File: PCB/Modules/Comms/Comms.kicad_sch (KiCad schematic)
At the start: 25 parts, among them J1 In, J2 ESP32, J3 Bus, J4 Bus, SW1 RUN/~{PROG}, U1 DS1390U, U2 THVD1420D, U3 WiFi / BLE, Y1 32.767kHz

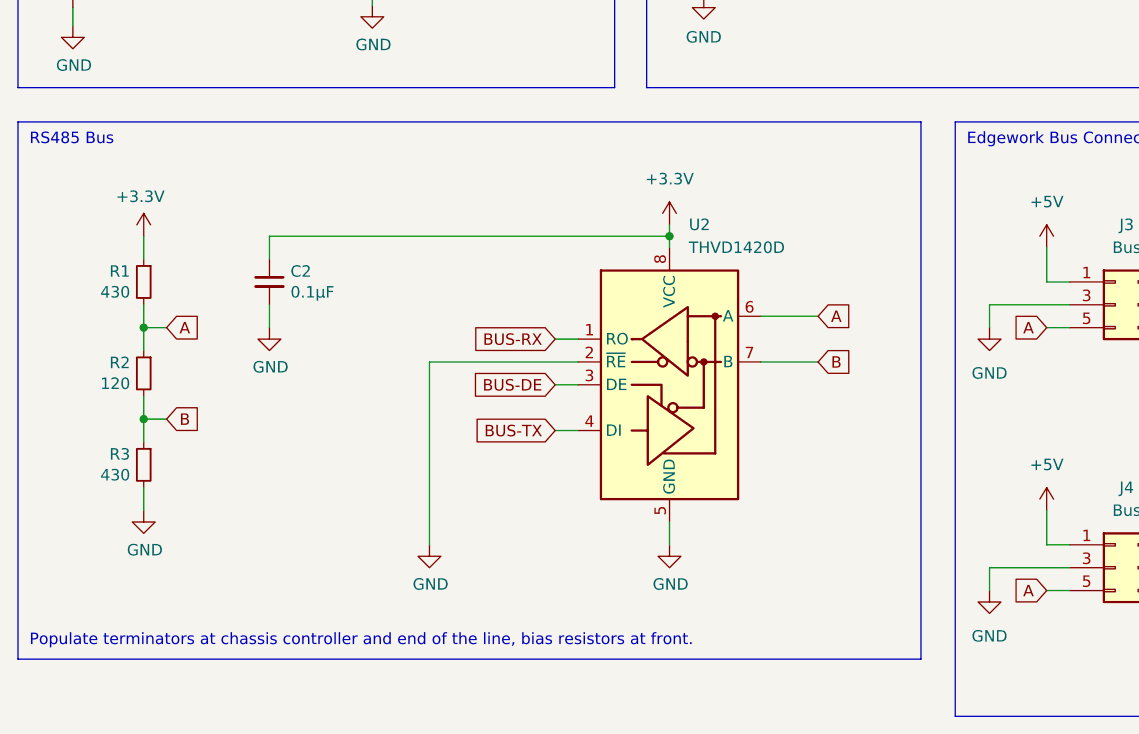
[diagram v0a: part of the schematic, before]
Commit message: Add ESD protection to the RS485 networks.
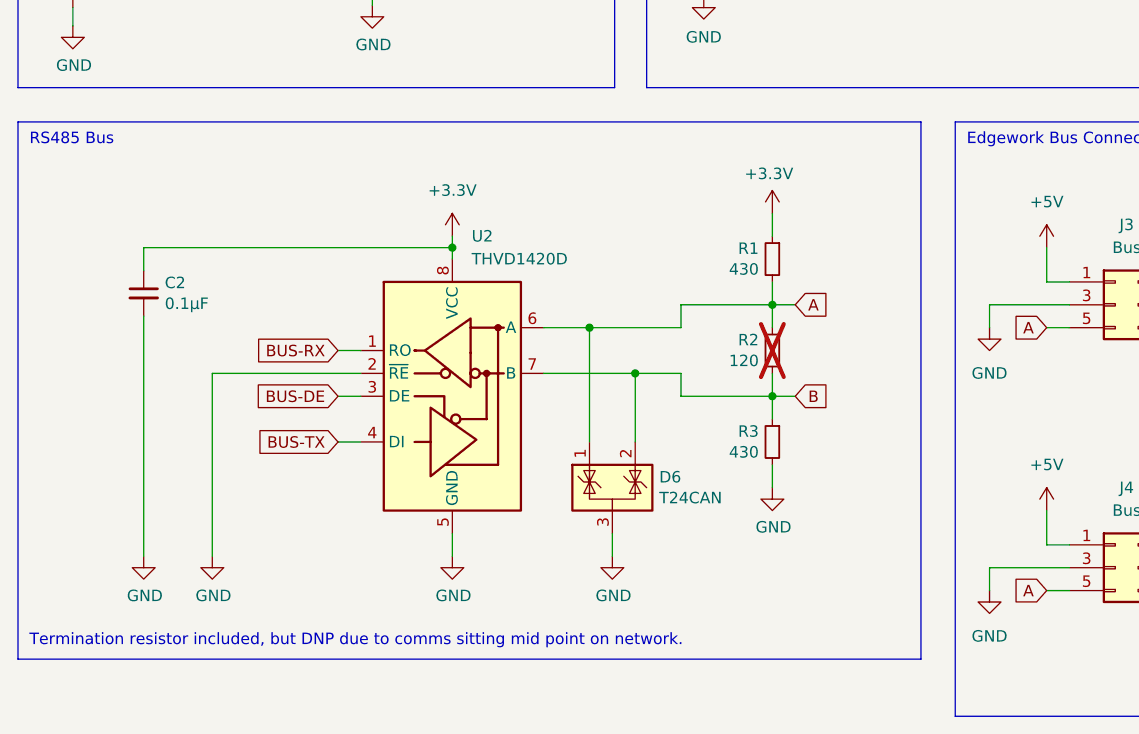
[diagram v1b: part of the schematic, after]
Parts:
- added D6: T24CAN, Package_TO_SOT_SMD:SOT-23, symbol Power_Protection:NUP2105L
- R2: now not fitted
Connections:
- net A: now also D6.1 (K)
- net B: now also D6.2 (K)
- net GND: now also D6.3 (A)
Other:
- note added: "Termination resistor included, but DNP due to comms sitting mid point on network."
- note removed: "Populate terminators at chassis controller and end of the line, bias resistors at front."
- moved on the sheet: C2, R1, R3, U2

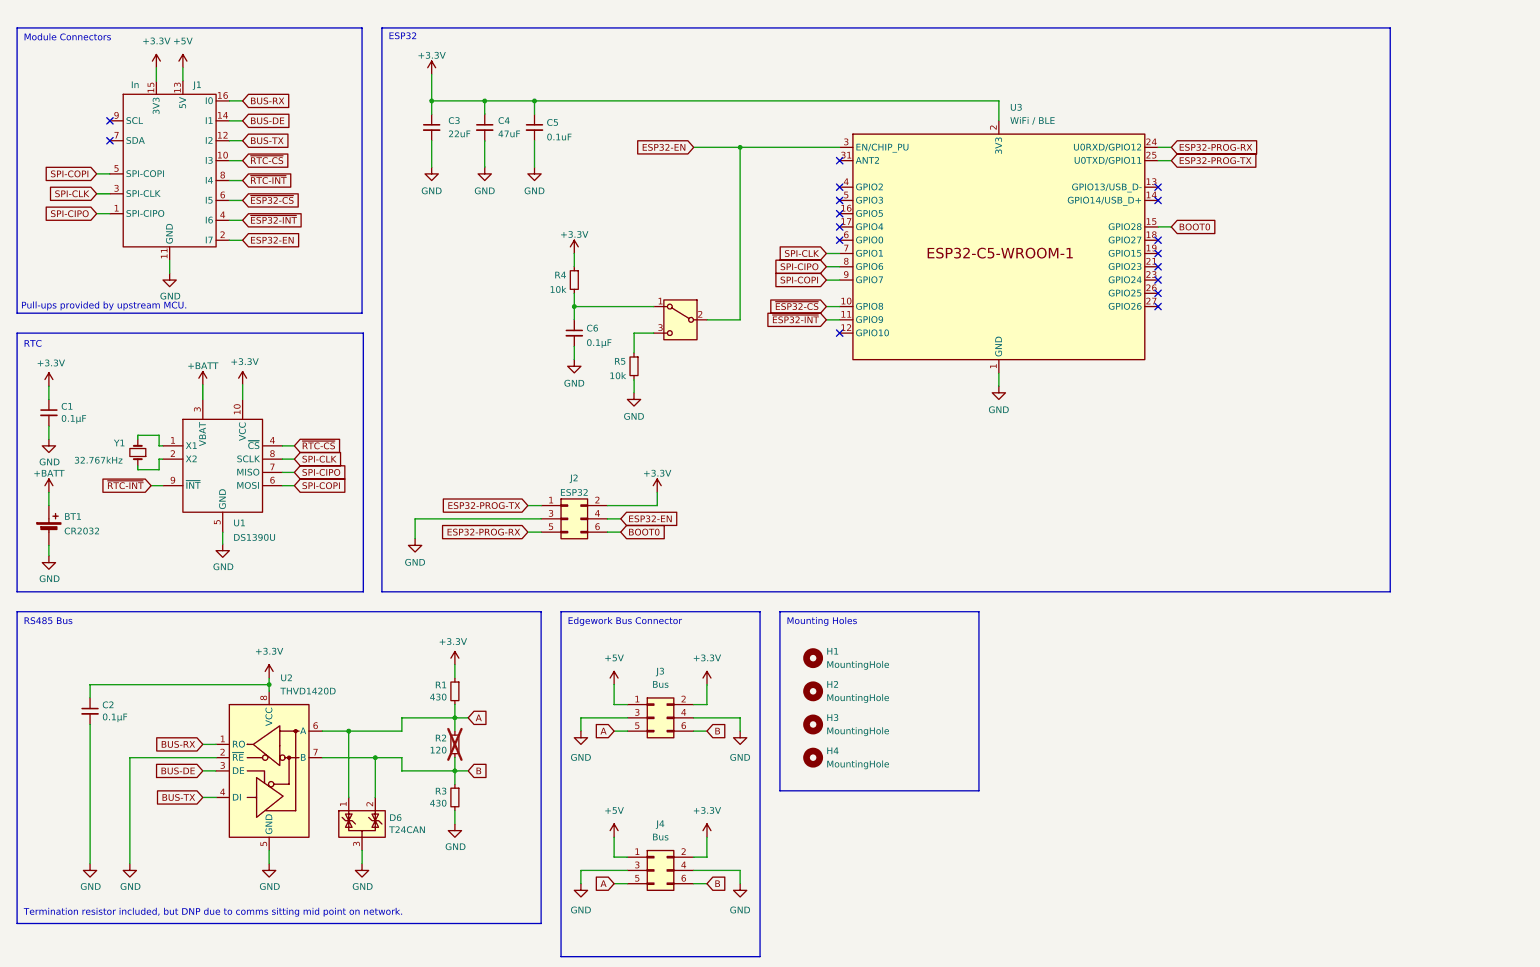
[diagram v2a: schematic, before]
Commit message: feat: Rework comms board to have an STM32 for communications.
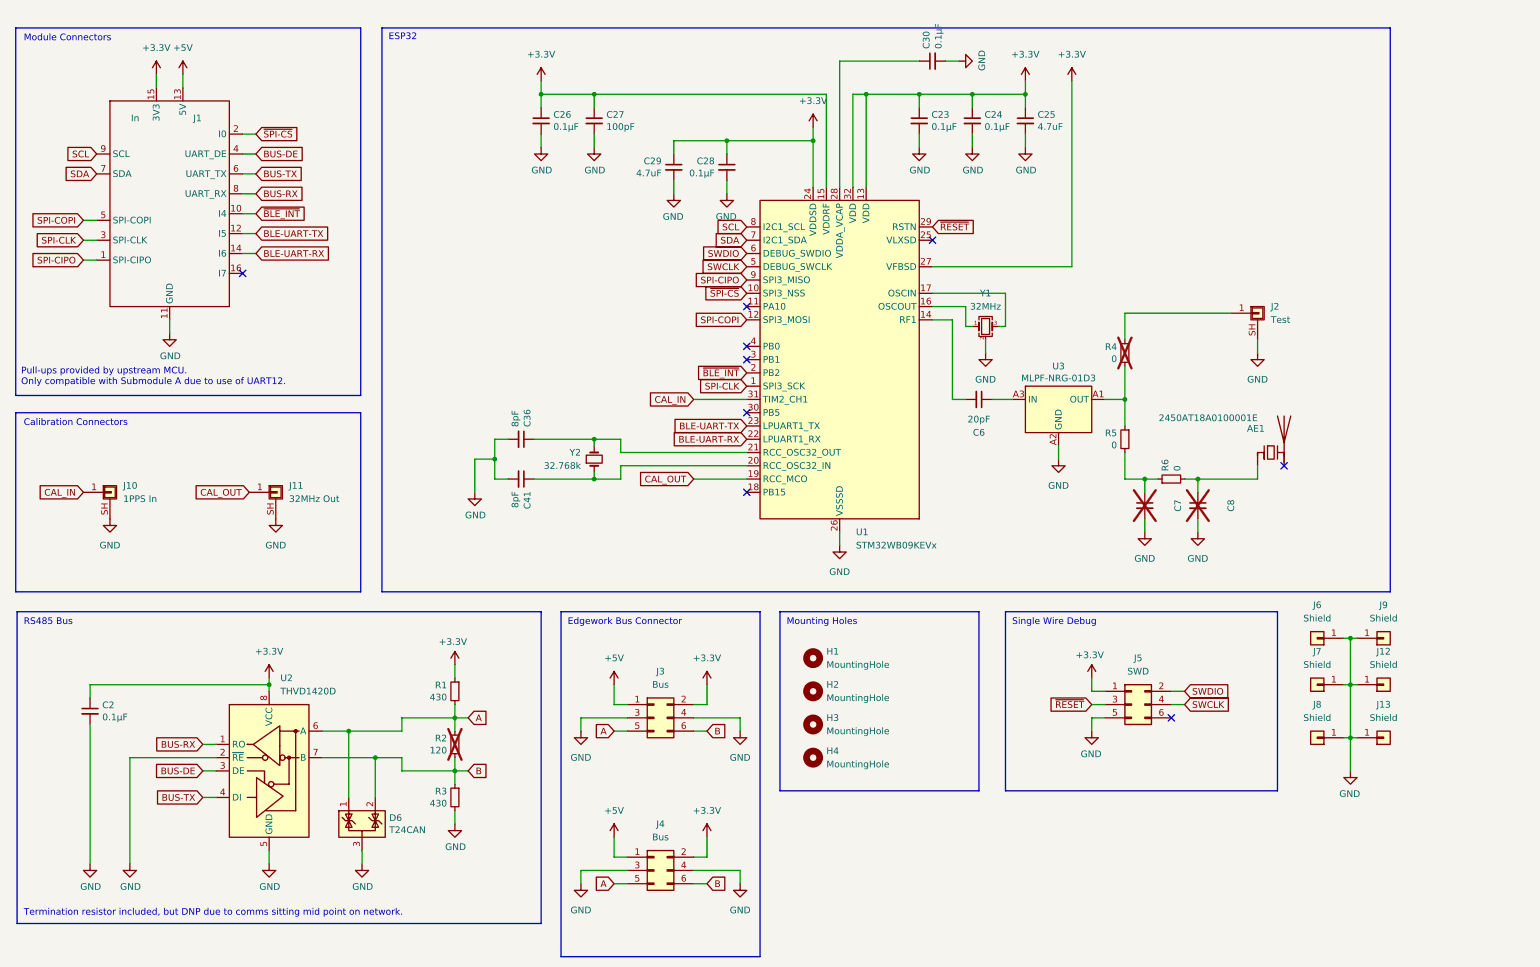
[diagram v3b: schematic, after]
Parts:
- removed BT1: CR2032, KTANE:CellHolder, symbol Device:Battery_Cell
- removed C1: 0.1μF, Capacitor_SMD:C_0603_1608Metric, symbol Device:C_Small
- removed C3: 22uF, Capacitor_SMD:C_1206_3216Metric, symbol Device:C_Small
- removed C4: 47uF, Capacitor_SMD:C_0603_1608Metric, symbol Device:C_Small
- removed C5: 0.1uF, Capacitor_SMD:C_0603_1608Metric, symbol Device:C_Small
- removed J2: ESP32, Connector:Tag-Connect_TC2030-IDC-NL_2x03_P1.27mm_Vertical, symbol Connector_Generic:Conn_02x03_Odd_Even
- removed SW1: RUN/~{PROG}, KTANE:JS102011JCQN, symbol Switch:SW_SPDT
- removed U1: DS1390U, Package_SO:MSOP-10_3x3mm_P0.5mm, symbol KTANE:DS1390U
- removed U3: WiFi / BLE, KTANE:ESP32-C5-WROOM-1U, symbol KTANE:ESP32-C5-WROOM-1U
- removed Y1: 32.767kHz, Crystal:Crystal_SMD_2012-2Pin_2.0x1.2mm, symbol Device:Crystal_Small
- added AE1: 2450AT18A0100001E, RF_Antenna:Johanson_2450AT18x100_2400-2500Mhz, symbol Device:Antenna_Chip
- added C23, C24, C26, C28, C30: 0.1μF, Capacitor_SMD:C_0603_1608Metric, symbol Device:C_Small
- added C25, C29: 4.7uF, Capacitor_SMD:C_0603_1608Metric, symbol Device:C_Small
- added C27: 100pF, Capacitor_SMD:C_0603_1608Metric, symbol Device:C_Small
- added C36, C41: 8pF, Capacitor_SMD:C_0603_1608Metric, symbol Device:C_Small
- added C7, C8: (no value), KTANE:R_0402_1005Metric_Tweaked, symbol Device:C_Small
- added J10: 1PPS In, Connector_Coaxial:U.FL_Hirose_U.FL-R-SMT-1_Vertical, symbol Connector_Generic_Shielded:Conn_01x01_Shielded
- added J11: 32MHz Out, Connector_Coaxial:U.FL_Hirose_U.FL-R-SMT-1_Vertical, symbol Connector_Generic_Shielded:Conn_01x01_Shielded
- added J12, J13: Shield, KTANE:EMI_Shield_Straight, symbol Connector_Generic:Conn_01x01
- added J2: Test, Connector_Coaxial:U.FL_Hirose_U.FL-R-SMT-1_Vertical, symbol Connector_Generic_Shielded:Conn_01x01_Shielded
- added J5: SWD, Connector:Tag-Connect_TC2030-IDC-NL_2x03_P1.27mm_Vertical, symbol Connector_Generic:Conn_02x03_Odd_Even
- added J6, J7, J8, J9: Shield, KTANE:EMI_Shield_Corner, symbol Connector_Generic:Conn_01x01
- added R6: 0, KTANE:R_0402_1005Metric_Tweaked, symbol Device:R_Small
- added U1: STM32WB09KEVx, Package_DFN_QFN:QFN-32-1EP_5x5mm_P0.5mm_EP3.7x3.7mm, symbol MCU_ST_STM32WB:STM32WB09KEVx
- added U3: MLPF-NRG-01D3, KTANE:MLPF-NRG-01D3, symbol KTANE:MLPF-NRG-01D3
- added Y1: 32MHz, Crystal:Crystal_SMD_2016-4Pin_2.0x1.6mm, symbol Device:Crystal_GND24_Small
- added Y2: 32.768k, Crystal:Crystal_SMD_2012-2Pin_2.0x1.2mm, symbol Device:Crystal_Small
- C6: value 0.1μF -> 20pF; footprint Capacitor_SMD:C_0603_1608Metric -> KTANE:R_0402_1005Metric_Tweaked; DIGIKEY 1276-1005-1-ND -> 1276-6601-1-ND
- H1, H2, H3, H4: footprint MountingHole:MountingHole_3.2mm_M3 -> KTANE:MountingHole_3.2mm_M3_NoCopper
- R4: value 10k -> 0; footprint Resistor_SMD:R_0603_1608Metric -> KTANE:R_0402_1005Metric_Tweaked; DIGIKEY P10.0KHCT-ND -> 10-ERJ-H2G0R00XCT-ND; now not fitted
- R5: value 10k -> 0; footprint Resistor_SMD:R_0603_1608Metric -> KTANE:R_0402_1005Metric_Tweaked; DIGIKEY P10.0KHCT-ND -> 10-ERJ-H2G0R00XCT-ND
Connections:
- net ~{ESP32-CS} is gone; now on net BUS-TX: J1.6 (I2)
- net ~{ESP32-INT} is gone; now on net BUS-DE: J1.4 (I1)
- net ~{RTC-INT} is gone; now on net BUS-RX: J1.8 (I3)
- net +3.3V: now also C23.1, C24.1, C25.1, C26.1, C27.1, C28.1, C29.1, J5.1 (Pin_1), U1.13 (VDD), U1.15 (VDDRF), U1.24 (VDDSD), U1.27 (VFBSD), U1.32 (VDD); no longer R4.1
- net BUS-DE: no longer J1.14 (I1)
- net BUS-RX: no longer J1.16 (I0)
- net BUS-TX: no longer J1.12 (I2)
- net GND: now also C23.2, C24.2, C25.2, C26.2, C27.2, C28.2, C29.2, C30.2, C36.2, C41.2, C7.2, C8.2, J10.SH (Shield), J11.SH (Shield), J12.1 (Pin_1), J13.1 (Pin_1), J2.SH (Shield), J5.5 (Pin_5), J6.1 (Pin_1), J7.1 (Pin_1), J8.1 (Pin_1), J9.1 (Pin_1), U1.26 (VSSSD), U3.A2 (GND), U3.B1 (GND), U3.B2 (GND), U3.B3 (GND), Y1.2 (G), Y1.4 (G); no longer C6.2, R5.2
- net SPI-CIPO: now also U1.9 (PA8)
- net SPI-CLK: now also U1.1 (PB3)
- net SPI-COPI: now also U1.12 (PA11)
- net at R5.1: now also R4.2, U3.A1 (OUT)
- net SDA: now reaches J1.7 (SDA)
- net SDA: now also U1.7 (PA1)
- net SCL: now reaches J1.9 (SCL)
- net SCL: now also U1.8 (PA0)
- net at C6.1: now also U3.A3 (IN); no longer R4.2
- net ESP32-EN renamed ~{SPI-CS}
- net ~{SPI-CS}: now also U1.10 (PA9)
- net ~{RTC-CS} renamed ~{BLE_INT}
- net ~{BLE_INT}: now also U1.2 (PB2)
- new net: U1.16 (OSCOUT), Y1.1
- new net: U1.17 (OSCIN), Y1.3
- new net: C41.1, U1.20 (PB13), Y2.1
- new net: C36.1, U1.21 (PB12), Y2.2
- new net: C6.2, U1.14 (RF1)
- new net: C30.1, U1.28 (VDDA_VCAP)
- new net: J2.1 (Pin_1), R4.1
- new net: C7.1, R5.2, R6.1
- new net: AE1.1 (FEED), C8.1, R6.2
- new net BLE-UART-RX: J1.14 (I6), U1.22 (PB7)
- new net BLE-UART-TX: J1.12 (I5), U1.23 (PB6)
- new net CAL_IN: J10.1 (Pin_1), U1.31 (PB4)
- new net CAL_OUT: J11.1 (Pin_1), U1.19 (PB14)
- new net SWCLK: J5.4 (Pin_4), U1.5 (PA3)
- new net SWDIO: J5.2 (Pin_2), U1.6 (PA2)
- new net ~{RESET}: J5.3 (Pin_3), U1.29 (RSTN)
- no-connect marks 17 -> 9
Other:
- note added: "Calibration Connectors"
- note added: "Pull-ups provided by upstream MCU. Only compatible with Submodule A due to use of UART12."
- note added: "Single Wire Debug"
- note removed: "Pull-ups provided by upstream MCU."
- note removed: "RTC"
- moved on the sheet: J1

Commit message: feat: Add support for battery for RTC on comms board.
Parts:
- added D1: BAT54S, Package_TO_SOT_SMD:SOT-23, symbol Diode:BAT54S
- added J14: BATT +, KTANE:Pad4x2, symbol Connector:Conn_01x01_Socket
- added J15: BATT -, KTANE:Pad4x2, symbol Connector:Conn_01x01_Socket
- added JP1: NO BATT, Jumper:SolderJumper-2_P1.3mm_Open_Pad1.0x1.5mm, symbol Jumper:Jumper_2_Open
- added Q1: Q_PMOS_GSD, Package_TO_SOT_SMD:SOT-23, symbol Transistor_FET:Q_PMOS_GSD
- added R7: 1000, Resistor_SMD:R_0603_1608Metric, symbol Device:R_Small
- added R8: 120, Resistor_SMD:R_0603_1608Metric, symbol Device:R_Small
- J10, J11, J2: symbol Connector_Generic_Shielded:Conn_01x01_Shielded -> KTANE:UFLConnector
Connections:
- net +3.3V: now also U1.4 (PB0), JP1.1 (A), Q1.3 (D), R7.1; no longer C23.1, C24.1, C25.1, C26.1, C27.1, C28.1, C29.1, J5.1 (Pin_1), U1.13 (VDD), U1.15 (VDDRF), U1.24 (VDDSD), U1.27 (VFBSD), U1.32 (VDD)
- net GND: now also J10.2 (Shield), J11.2 (Shield), J2.2 (Shield), J15.1 (Pin_1); no longer J10.SH (Shield), J11.SH (Shield), J2.SH (Shield)
- net ~{RUN}: now reaches U1.30 (PB5)
- net ~{RUN}: now also R8.2
- new net: D1.3 (COM), J14.1 (Pin_1), JP1.2 (B)
- new net: Q1.1 (G), R8.1
- new net: D1.1 (A), R7.2
- new net +3.3VP: C23.1, C24.1, C25.1, C26.1, C27.1, C28.1, C29.1, D1.2 (K), J5.1 (Pin_1), Q1.2 (S), U1.13 (VDD), U1.15 (VDDRF), U1.24 (VDDSD), U1.27 (VFBSD), U1.32 (VDD)
- no-connect marks 9 -> 7
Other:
- title: KTANE Physical Edition - SPI 2.4Ghz Radio / SD Card / RTC -> KTANE Physical Edition - Edgework Bus / BLE
- moved on the sheet: AE1, C23, C24, C25, C26, C27, C28, C29, C30, C36, C41, C6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
